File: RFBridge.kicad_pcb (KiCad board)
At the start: 4 copper layers, 34 parts, among them U1 CC2520, U2 CC2592, U3 CC1120, U4 CC1190, U5 LDB182G4520C-110, U6 0900PC15J0013

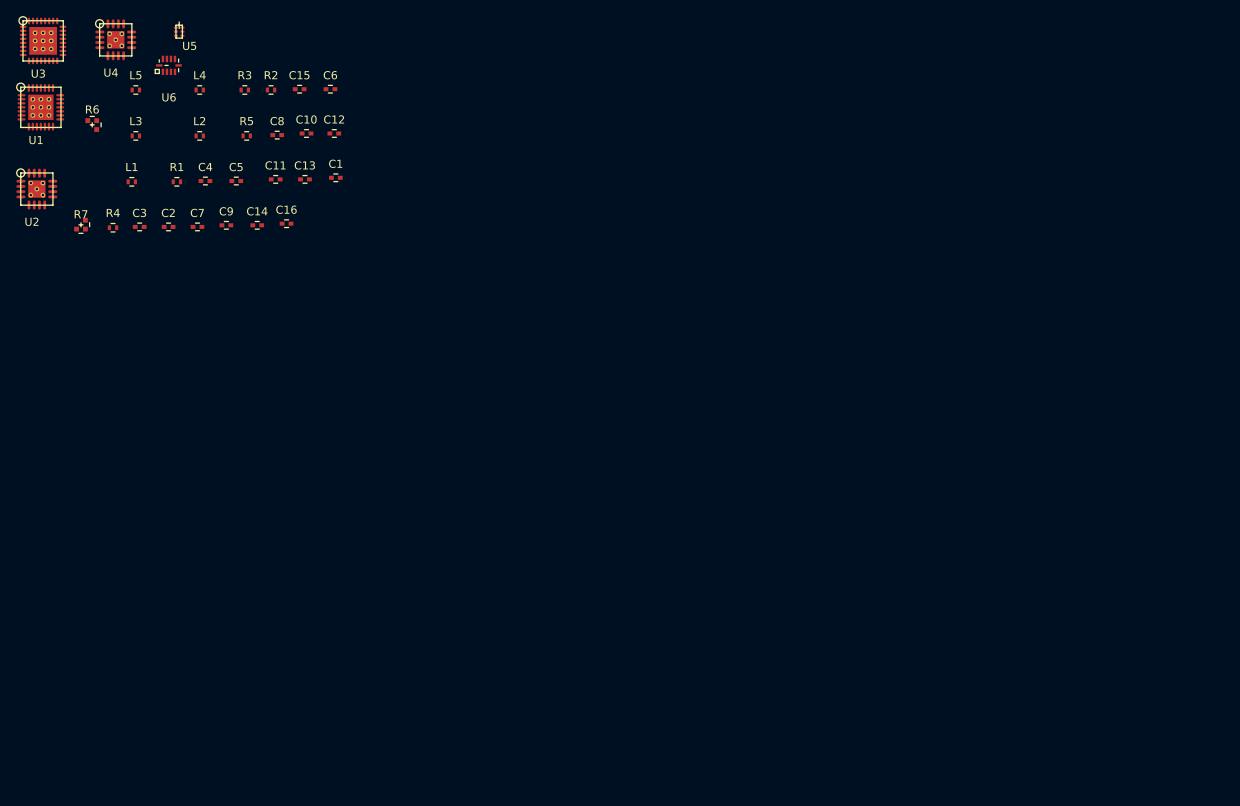
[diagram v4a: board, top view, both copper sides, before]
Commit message: Finished schematic of 2.4GHz and 900MHz radios
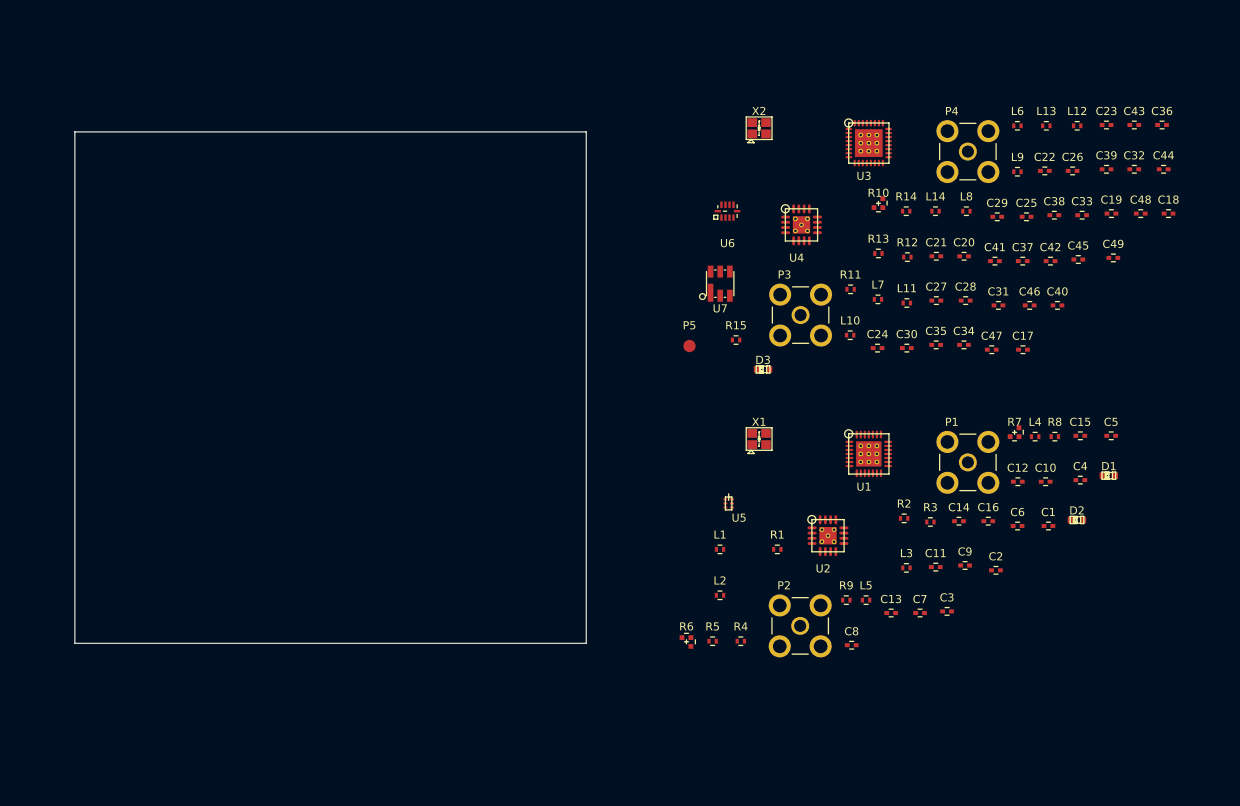
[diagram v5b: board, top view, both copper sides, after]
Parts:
- added C17: 220p, Capacitors_SMD:C_0402, F.Cu at (155.8, 65.1)
- added C18: 10u, Capacitors_SMD:C_0402, F.Cu at (173.9, 48.2)
- added C19: 0.8p, Capacitors_SMD:C_0402, F.Cu at (166.8, 48.2)
- added C20: 15p, Capacitors_SMD:C_0402, F.Cu at (148.5, 53.5)
- added C21: 27p, Capacitors_SMD:C_0402, F.Cu at (145.1, 53.5)
- added C22: 12p, Capacitors_SMD:C_0402, F.Cu at (158.5, 42.9)
- added C23: 47p, Capacitors_SMD:C_0402, F.Cu at (166.2, 37.2)
- added C24: 1u, Capacitors_SMD:C_0402, F.Cu at (137.8, 64.9)
- added C25: 47p, Capacitors_SMD:C_0402, F.Cu at (156.3, 48.6)
- added C26: 1n, Capacitors_SMD:C_0402, F.Cu at (162.0, 42.9)
- added C27: 12p, Capacitors_SMD:C_0402, F.Cu at (145.1, 59.0)
- added C28: 3.3p, Capacitors_SMD:C_0402, F.Cu at (148.7, 59.0)
- added C29: 7.5p, Capacitors_SMD:C_0402, F.Cu at (152.6, 48.6)
- added C30: 9.1n, Capacitors_SMD:C_0402, F.Cu at (141.4, 64.9)
- added C31: 220n, Capacitors_SMD:C_0402, F.Cu at (152.8, 59.6)
- added C32: 47n, Capacitors_SMD:C_0402, F.Cu at (169.6, 42.7)
- added C33: 47n, Capacitors_SMD:C_0402, F.Cu at (163.2, 48.4)
- added C34: 47n, Capacitors_SMD:C_0402, F.Cu at (148.5, 64.5)
- added C35: 47n, Capacitors_SMD:C_0402, F.Cu at (145.0, 64.5)
- added C36: 47n, Capacitors_SMD:C_0402, F.Cu at (173.1, 37.2)
- added C37: 47n, Capacitors_SMD:C_0402, F.Cu at (155.8, 54.1)
- added C38: 47n, Capacitors_SMD:C_0402, F.Cu at (159.7, 48.4)
- added C39: 47n, Capacitors_SMD:C_0402, F.Cu at (166.2, 42.7)
- added C40: 47n, Capacitors_SMD:C_0402, F.Cu at (160.1, 59.6)
- added C41: 47n, Capacitors_SMD:C_0402, F.Cu at (152.3, 54.1)
- added C42: 12p, Capacitors_SMD:C_0402, F.Cu at (159.2, 54.1)
- added C43: 33p, Capacitors_SMD:C_0402, F.Cu at (169.6, 37.2)
- added C44: 1.8n, Capacitors_SMD:C_0402, F.Cu at (173.3, 42.7)
- added C45: 10n, Capacitors_SMD:C_0402, F.Cu at (162.7, 53.9)
- added C46: 12p, Capacitors_SMD:C_0402, F.Cu at (156.6, 59.6)
- added C47: 10n, Capacitors_SMD:C_0402, F.Cu at (151.9, 65.1)
- added C48: 47n, Capacitors_SMD:C_0402, F.Cu at (170.4, 48.2)
- added C49: 100p, Capacitors_SMD:C_0402, F.Cu at (167.0, 53.7)
- added D1: LED, LEDs:LED-0603, F.Cu at (166.5, 80.8)
- added D2: LED, LEDs:LED-0603, F.Cu at (162.5, 86.3)
- added D3: LED, LEDs:LED-0603, F.Cu at (123.5, 67.6)
- added L10: 22n, Resistors_SMD:R_0402, F.Cu at (134.4, 63.3)
- added L11: 7.5n, Resistors_SMD:R_0402, F.Cu at (141.4, 59.3)
- added L12: 2.9n, Resistors_SMD:R_0402, F.Cu at (162.6, 37.3)
- added L13: 9.1n, Resistors_SMD:R_0402, F.Cu at (158.7, 37.3)
- added L14: 8.2n, Resistors_SMD:R_0402, F.Cu at (145.0, 47.9)
- added L6: 11n, Resistors_SMD:R_0402, F.Cu at (155.1, 37.3)
- added L7: 10n, Resistors_SMD:R_0402, F.Cu at (137.8, 58.9)
- added L8: 1.5n, Resistors_SMD:R_0402, F.Cu at (148.8, 47.9)
- added L9: 15n, Resistors_SMD:R_0402, F.Cu at (155.1, 43.0)
- added P1: BNC, Connect:SMB_Straight, F.Cu at (149.0, 79.1)
- added P2: BNC, Connect:SMB_Straight, F.Cu at (128.2, 99.4)
- added P3: BNC, Connect:SMB_Straight, F.Cu at (128.2, 60.8)
- added P4: BNC, Connect:SMB_Straight, F.Cu at (149.0, 40.5)
- added P5: TST, Measurement_Points:Measurement_Point_Round-SMD-Pad_Small, F.Cu at (114.4, 64.7)
- added R10: 0, Resistors_SMD:R3_LH_0402, F.Cu at (137.9, 47.5)
- added R11: 47, Resistors_SMD:R_0402, F.Cu at (134.4, 57.6)
- added R12: 3.3k, Resistors_SMD:R_0402, F.Cu at (141.5, 53.6)
- added R13: 2k, Resistors_SMD:R_0402, F.Cu at (137.9, 53.2)
- added R14: 56k, Resistors_SMD:R_0402, F.Cu at (141.3, 47.9)
- added R15: 10, Resistors_SMD:R_0402, F.Cu at (120.2, 63.9)
- added R8: 2k, Resistors_SMD:R_0402, F.Cu at (159.8, 75.9)
- added R9: 2k, Resistors_SMD:R_0402, F.Cu at (133.9, 96.2)
- added U7: EPCOS_B3588, SMD_Packages:DCC6C, F.Cu at (118.2, 56.9)
- added X1: FA-20H32.0000MF20X-K3, Crystals_Oscillators_SMD:FA-20H, F.Cu at (123.1, 76.2)
- added X2: FA-20H32.0000MF20X-K3, Crystals_Oscillators_SMD:FA-20H, F.Cu at (123.1, 37.6)
- L1, L2: value INDUCTOR -> FERRITE BEAD
- L3: value INDUCTOR -> 4.7n
- L4: value INDUCTOR -> 1n
- L5: value INDUCTOR -> 2n
- R6: value R3-RH -> 0
- R7: value R3-LH -> 0
- moved R7 118.7 mm to (154.8, 75.9)
- moved C4 114.8 mm to (162.9, 81.3)
- moved C5 113.1 mm to (166.8, 75.8)
- moved L4 112.3 mm to (157.3, 75.9)
- moved U1 111.4 mm to (136.7, 78.1)
- moved C2 111.2 mm to (152.5, 92.5)
- moved C3 111.0 mm to (146.4, 97.6)
- moved L5 110.6 mm to (136.3, 96.2)
- moved L3 109.7 mm to (141.4, 92.2)
- moved U2 107.2 mm to (131.6, 88.2)
- moved C15 106.1 mm to (162.9, 75.8)
- moved U3 103.3 mm to (136.7, 39.5)
- moved C7 101.7 mm to (143.0, 97.8)
- moved C10 101.4 mm to (158.6, 81.5)
- moved C6 101.1 mm to (155.2, 87.0)
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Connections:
- net Net-(R2-Pad2) renamed /2G4Radio/HGM
- net Net-(R3-Pad2) renamed /2G4Radio/LNA_EN
- net Net-(R4-Pad2) renamed /2G4Radio/PA_EN
- net Net-(U1-Pad1) renamed /2G4Radio/MISO
- net Net-(U1-Pad2) renamed /2G4Radio/MOSI
- net Net-(U1-Pad25) renamed /2G4Radio/RESET_L
- net Net-(U1-Pad26) renamed /2G4Radio/VREG_EN
- net Net-(U1-Pad28) renamed /2G4Radio/SCLK
- net Net-(U1-Pad6) renamed /2G4Radio/CCA
- net Net-(U1-Pad7) renamed /2G4Radio/FIFOP
- net Net-(U3-Pad10) renamed /900MRadio/GPIO0
- net Net-(U3-Pad11) renamed /900MRadio/CS_L
- net Net-(U3-Pad2) renamed /900MRadio/RESET_L
- net Net-(U3-Pad4) renamed /900MRadio/GPIO2
- net Net-(U3-Pad7) renamed /900MRadio/MOSI
- net Net-(U3-Pad8) renamed /900MRadio/SCLK
- net Net-(U3-Pad9) renamed /900MRadio/MISO
- net Net-(U4-Pad6) renamed /900MRadio/HGM
- net Net-(U4-Pad7) renamed /900MRadio/LNA_EN
- net Net-(U4-Pad8) renamed /900MRadio/PA_EN
- U1 pad 3: (no net) -> /2G4Radio/CS_L
- U1 pad 4: Net-(U1-Pad4) -> GND
- U1 pad 5: Net-(U1-Pad5) -> /2G4Radio/SFD
- U1 pad 9: Net-(U1-Pad9) -> /2G4Radio/FIFO
- U3 pad 1: Net-(U3-Pad1) -> /900MRadio/VDD_CC1120
- U3 pad 12: Net-(U3-Pad12) -> /900MRadio/VDD_CC1120
- U3 pad 13: Net-(U3-Pad13) -> /900MRadio/VDD_CC1120
- U3 pad 15: Net-(U3-Pad15) -> /900MRadio/VDD_CC1120
- U3 pad 17: Net-(U3-Pad17) -> Net-(L14-Pad2)
- U3 pad 22: Net-(U3-Pad22) -> /900MRadio/VDD_CC1120
- U3 pad 25: Net-(U3-Pad25) -> /900MRadio/VDD_CC1120
- U3 pad 27: Net-(U3-Pad27) -> /900MRadio/VDD_CC1120
- U3 pad 28: Net-(U3-Pad28) -> /900MRadio/VDD_CC1120
- U3 pad 3: Net-(U3-Pad3) -> /900MRadio/GPIO3
- U3 pad 5: Net-(U3-Pad5) -> /900MRadio/VDD_CC1120
- U4 pad 10: Net-(U4-Pad10) -> Net-(L7-Pad2)
- U4 pad 11: Net-(U4-Pad11) -> Net-(L7-Pad2)
- U6 pad 1: Net-(U6-Pad1) -> Net-(U3-Pad20)
- U6 pad 10: Net-(U6-Pad10) -> GND
- U6 pad 2: Net-(U6-Pad2) -> Net-(U3-Pad19)
- U6 pad 3: Net-(U6-Pad3) -> Net-(U3-Pad18)
- U6 pad 4: Net-(U6-Pad4) -> Net-(L14-Pad2)
- U6 pad 5: Net-(U6-Pad5) -> GND
- U6 pad 6: Net-(U6-Pad6) -> GND
- U6 pad 8: Net-(U6-Pad8) -> GND
- U6 pad 9: Net-(U6-Pad9) -> GND
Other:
- board outline added: 63.5 x 63.5 mm

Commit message: Updated layout
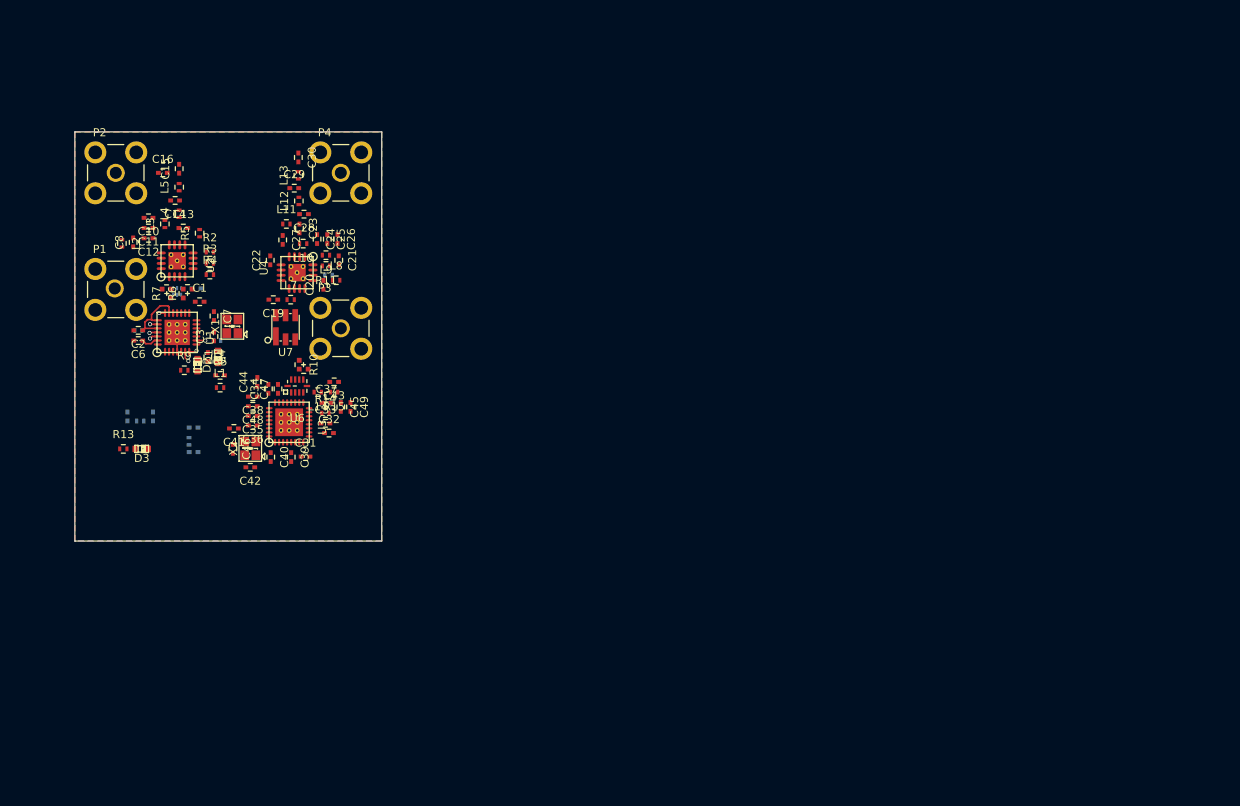
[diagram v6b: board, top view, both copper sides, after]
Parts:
- removed P5: TST, Measurement_Points:Measurement_Point_Round-SMD-Pad_Small
- added C50: 100n, Capacitors_SMD:C_0402, B.Cu at (52.8, 77.9)
- added C51: 2u2, Capacitors_SMD:C_0402, B.Cu at (52.8, 74.8)
- added L15: FERRITE BEAD, Resistors_SMD:R_0402, B.Cu at (52.3, 76.5)
- C17, C18, C9, L6, R1, R12, R8, U5: moved to B.Cu
- U2: footprint SMD_Packages:RGV_S-PVQFN-N16 -> RGV_S-PVQFN-N16
- moved C18 128.6 mm to (47.8, 73.4), turned to 90 degrees
- moved C36 118.9 mm to (60.2, 74.5), turned to 180 degrees
- moved C15 116.7 mm to (51.1, 42.7), turned to 90 degrees
- moved C10 116.1 mm to (47.2, 48.8), turned to 180 degrees
- moved C44 115.6 mm to (60.8, 69.1), turned to 90 degrees
- moved L6 114.9 mm to (46.2, 74.0)
- moved C48 112.8 mm to (60.2, 72.2), turned to 180 degrees
- moved C12 112.1 mm to (47.2, 51.3), turned to 180 degrees
- moved D1 111.6 mm to (55.9, 66.0), turned to 90 degrees
- moved C6 111.6 mm to (46.0, 64.0), turned to 180 degrees
- moved C17 111.5 mm to (44.6, 73.4), turned to 90 degrees
- moved C16 111.2 mm to (49.0, 43.2)
- moved C5 110.9 mm to (56.1, 68.3)
- moved D2 110.9 mm to (53.3, 67.1), turned to 270 degrees
- moved C2 110.6 mm to (46.0, 62.7), turned to 180 degrees
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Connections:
- net /900MRadio/VDD_CC1120 renamed /900MRadio/VDD_CC1120_ISO
- net Net-(C18-Pad2) renamed /900MRadio/CC11990_VDD_ISO
- U1 pad 17: Net-(R7-Pad2) -> Net-(R6-Pad1)
- U1 pad 19: Net-(R6-Pad2) -> Net-(R7-Pad1)
- U2 pad 2: Net-(R6-Pad1) -> Net-(R7-Pad2)
- U2 pad 3: Net-(R7-Pad1) -> Net-(R6-Pad2)
- U5 pad 4: Net-(R7-Pad3) -> Net-(R6-Pad3)
- U5 pad 6: Net-(R6-Pad3) -> Net-(R7-Pad3)
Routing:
- net AVDD: track 0.00 -> 8.96 mm
- net GND: track 0.00 -> 2.40 mm
- net Net-(C6-Pad1): track 0.00 -> 2.20 mm
- net /2G4Radio/CCA: track 0.00 -> 1.32 mm, vias 0 -> 1
- net /2G4Radio/FIFO: track 0.00 -> 1.10 mm, vias 0 -> 1
- net /2G4Radio/RESET_L: track 0.00 -> 1.09 mm, vias 0 -> 1
- net /2G4Radio/VREG_EN: track 0.00 -> 1.07 mm, vias 0 -> 1
- net Net-(R1-Pad1): track 0.00 -> 0.97 mm, vias 0 -> 1
- net /2G4Radio/FIFOP: track 0.00 -> 0.96 mm, vias 0 -> 1
- net Net-(U1-Pad21): track 0.00 -> 0.73 mm, vias 0 -> 1
- added copper zone on B.Cu, net GND
- added copper zone on F.Cu, net GND
- added copper zone on In1.Cu, net GND
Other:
- board size 63.5 x 63.5 mm -> 38.1 x 50.8 mm
- net class Default: clearance 0.2 -> 0.1524; trace_width 0.25 -> 0.1524; via_dia 0.6 -> 0.3556; via_drill 0.4 -> 0.254
- rule trace_clearance: 0.2 -> 0.1524
- rule trace_min: 0.2 -> 0.127
- rule via_min_drill: 0.3 -> 0.254
- rule via_min_size: 0.4 -> 0.3556

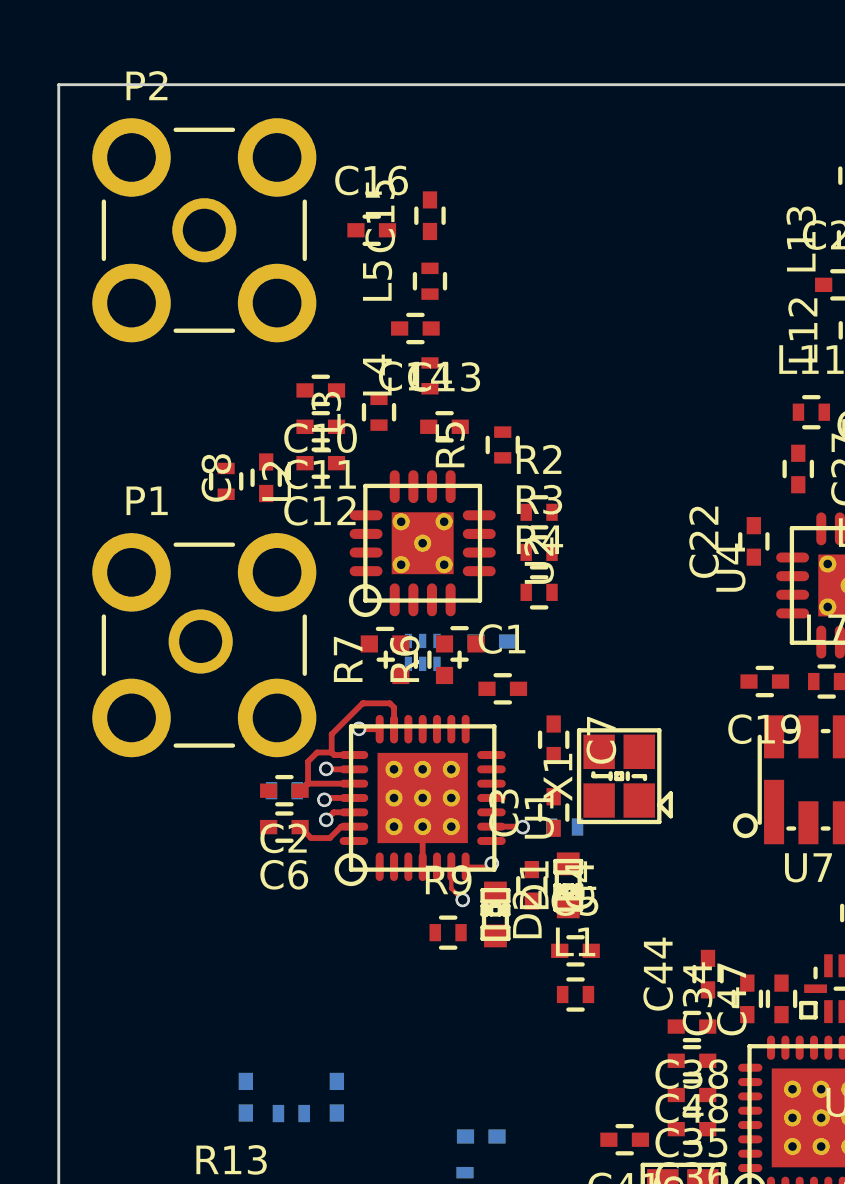
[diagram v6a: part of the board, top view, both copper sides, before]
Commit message: Fixed broken AVDD reference.
Routed 2.4GHz radio.
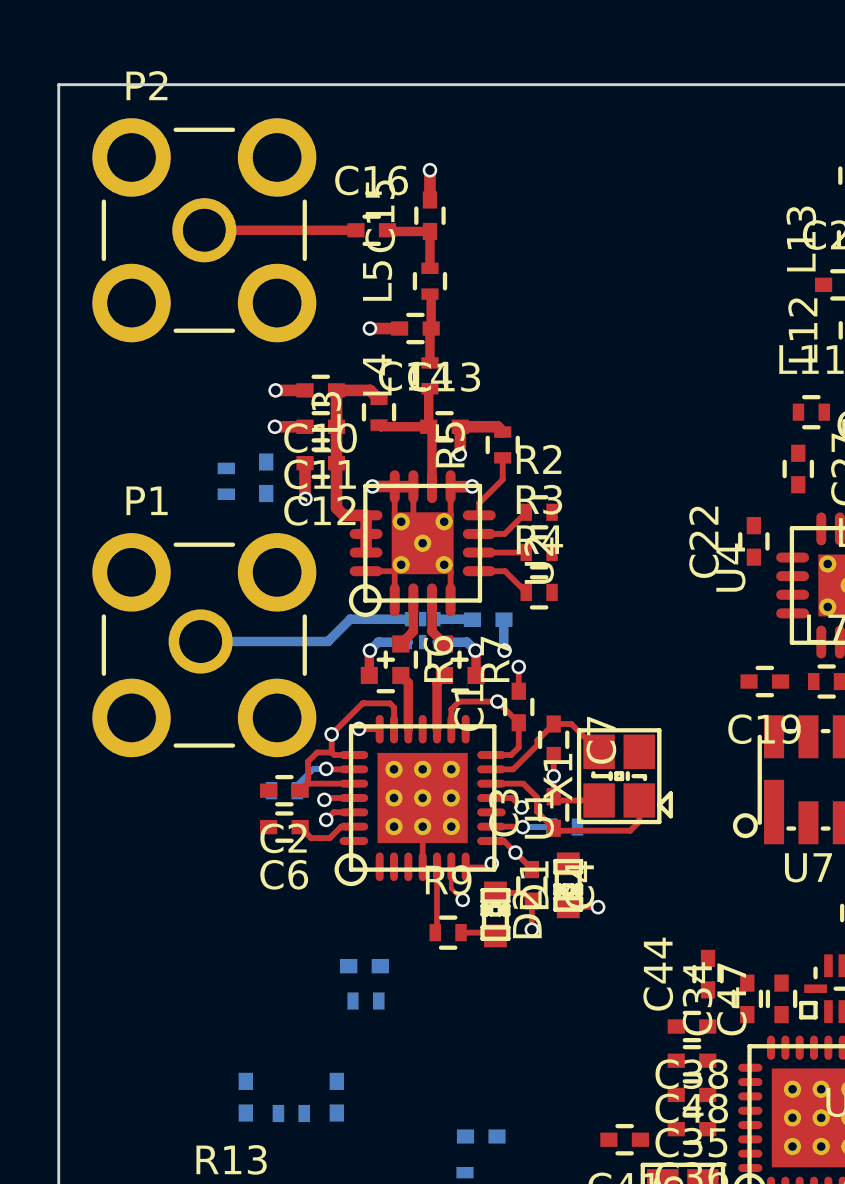
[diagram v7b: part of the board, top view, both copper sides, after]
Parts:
- C5, C8, L1, L2: moved to B.Cu
- moved C5 7.39 mm to (48.8, 68.9)
- moved L1 7.32 mm to (48.8, 70.1)
- moved R6 1.52 mm to (50.0, 58.2), turned to 270 degrees
- moved R7 1.52 mm to (51.6, 58.2), turned to 270 degrees
- moved C1 0.85 mm to (54.2, 59.8), turned to 90 degrees
- moved C9 0.77 mm to (53.1, 56.8)
- moved U5 0.76 mm to (50.8, 57.1)
- turned C8 to 270 degrees
- turned L2 to 90 degrees
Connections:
- net AVDD renamed /2G4Radio/VDD_CC2520_ISO
- net Net-(C10-Pad1) renamed /2G4Radio/VDD_CC2592_ISO
- U1 pad 17: Net-(R6-Pad1) -> Net-(R7-Pad2)
- U1 pad 19: Net-(R7-Pad1) -> Net-(R6-Pad2)
- U1 pad 23: Net-(R1-Pad1) -> Net-(U1-Pad23)
- U1 pad 27: Net-(C6-Pad1) -> Net-(U1-Pad27)
- U2 pad 2: Net-(R7-Pad2) -> Net-(R6-Pad1)
- U2 pad 3: Net-(R6-Pad2) -> Net-(R7-Pad1)
- U5 pad 4: Net-(R6-Pad3) -> Net-(R7-Pad3)
- U5 pad 6: Net-(R7-Pad3) -> Net-(R6-Pad3)
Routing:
- net GND: track 2.40 -> 35.0 mm, vias 0 -> 13
- net /2G4Radio/VDD_CC2520_ISO: track 8.96 -> 17.4 mm, vias 0 -> 4
- net /2G4Radio/VDD_CC2592_ISO: track 0.00 -> 8.15 mm
- net Net-(P1-Pad1): track 0.00 -> 7.60 mm
- net Net-(C3-Pad1): track 0.00 -> 6.88 mm
- net Net-(C16-Pad1): track 0.00 -> 5.29 mm
- net Net-(C13-Pad1): track 0.00 -> 5.24 mm
- net Net-(C7-Pad1): track 0.00 -> 4.91 mm
- net Net-(C15-Pad1): track 0.00 -> 2.79 mm
- net Net-(C14-Pad1): track 0.00 -> 2.44 mm
- net Net-(R5-Pad1): track 0.00 -> 2.34 mm
- net Net-(R7-Pad3): track 0.00 -> 2.34 mm, vias 0 -> 1
- net Net-(R6-Pad3): track 0.00 -> 2.34 mm, vias 0 -> 1
- net /2G4Radio/SFD: track 0.00 -> 2.32 mm
- net Net-(R7-Pad2): track 0.00 -> 1.98 mm
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- added copper zone on In2.Cu, net /2G4Radio/VDD_CC2520_ISO
- added copper zone on In2.Cu, net GND
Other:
- net class 50ohm added: clearance 0.3302, trace_width 0.3302, via_dia 0.3556, via_drill 0.254

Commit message: Mostly finished up 900MHz routing.
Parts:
- C47: moved to B.Cu
- moved R13 21.5 mm to (65.4, 80.4)
- moved D3 21.5 mm to (67.7, 80.4)
- moved C44 1.56 mm to (62.0, 70.0)
- moved C47 1.40 mm to (64.3, 69.0)
- moved C34 1.24 mm to (63.3, 69.7)
- moved C33 0.44 mm to (69.7, 74.3)
- moved R12 0.15 mm to (69.7, 55.9)
- moved C32 0.08 mm to (69.7, 75.6)
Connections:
- net /900MRadio/CC11990_VDD_ISO renamed /900MRadio/VDD_CC1190_ISO
- U1 pad 23: Net-(U1-Pad23) -> Net-(R1-Pad1)
- U1 pad 27: Net-(U1-Pad27) -> Net-(C6-Pad1)
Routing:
- net GND: track 35.0 -> 69.2 mm, vias 13 -> 27
- net /900MRadio/VDD_CC1120_ISO: track 0.00 -> 26.6 mm, vias 0 -> 9
- net /2G4Radio/VDD_CC2520_ISO: track 17.4 -> 29.5 mm
- net /900MRadio/VDD_CC1190_ISO: track 0.00 -> 9.90 mm
- net Net-(P3-Pad1): track 0.00 -> 8.45 mm
- net Net-(C30-Pad2): track 0.00 -> 6.55 mm
- net Net-(C46-Pad1): track 0.00 -> 5.76 mm
- net Net-(C42-Pad1): track 0.00 -> 5.35 mm
- net /900MRadio/GPIO3: track 0.00 -> 4.78 mm
- net Net-(C41-Pad1): track 0.00 -> 4.31 mm
- net Net-(C22-Pad2): track 0.00 -> 4.27 mm
- net Net-(L7-Pad2): track 0.00 -> 3.71 mm
- net Net-(C23-Pad1): track 0.00 -> 3.63 mm
- net Net-(R10-Pad1): track 0.00 -> 3.30 mm
- net Net-(C19-Pad1): track 0.00 -> 3.16 mm
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- added copper zone on In2.Cu, net /900MRadio/VDD_CC1120_ISO
